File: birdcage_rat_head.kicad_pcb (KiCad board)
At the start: 2 copper layers, 131.9 x 63.3 mm, 40 parts, among them J1 Conn_Coaxial_0, J2 Conn_Coaxial_90

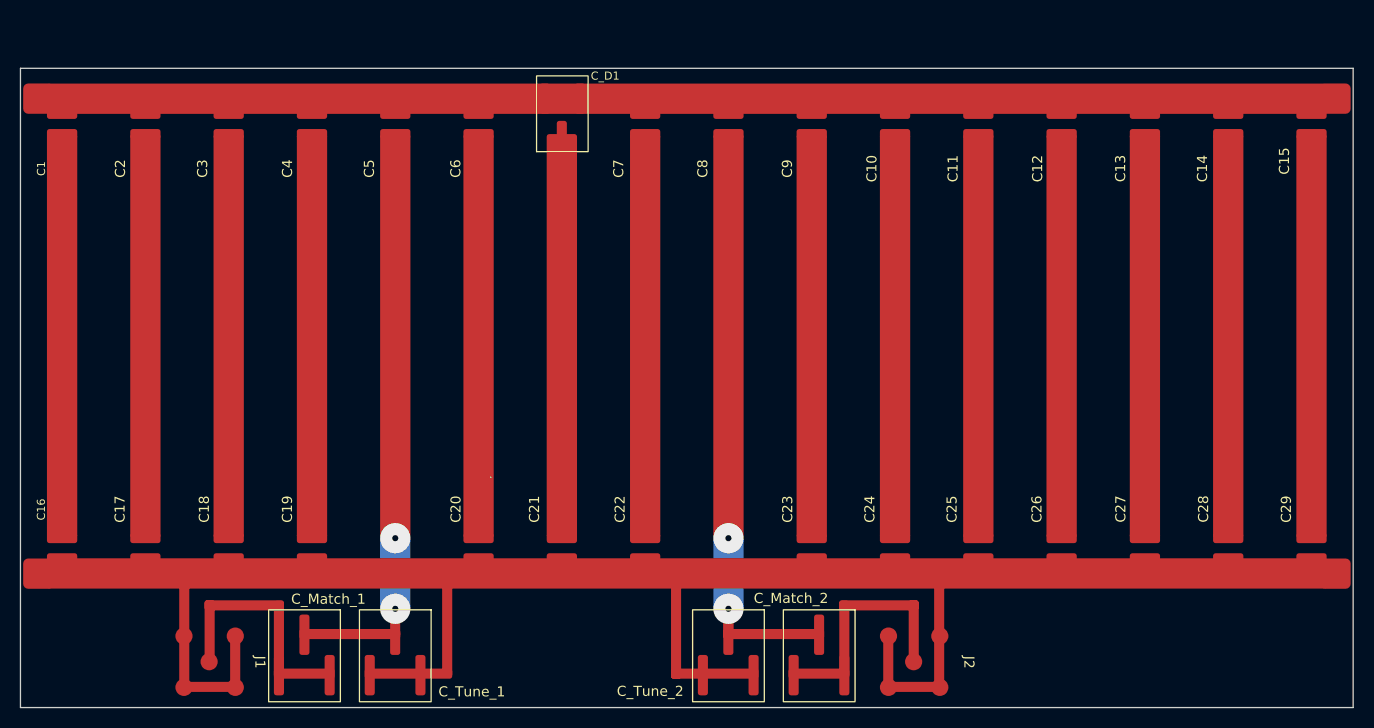
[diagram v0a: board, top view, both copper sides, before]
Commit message: Accounted for PCB thickness and reduced gap between flange and pcb
Gap was reduced so that more of the rat brain is in the coil.
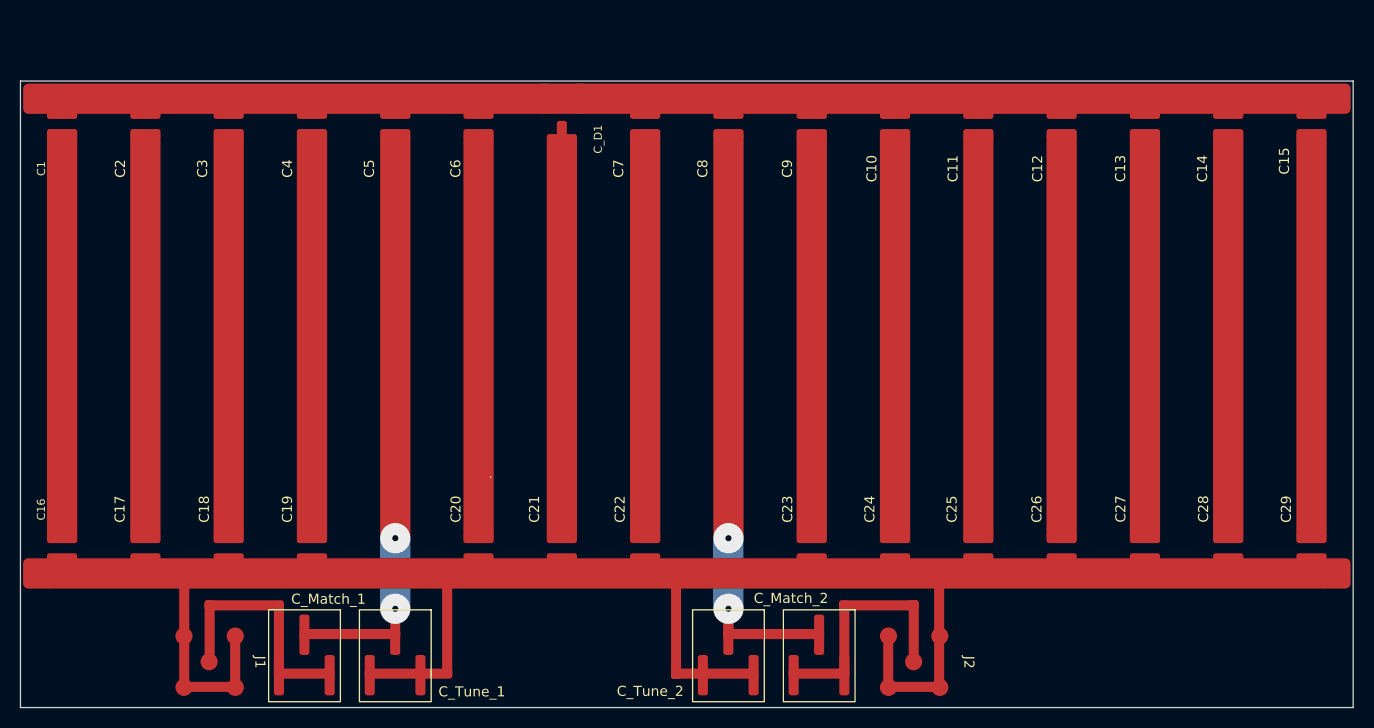
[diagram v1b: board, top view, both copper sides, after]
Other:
- board size 131.9 x 63.3 mm -> 131.9 x 62 mm
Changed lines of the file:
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@@
 	(footprint "custom_footprints:pad"
 		(layer "F.Cu")
-		(at 64.24 44.31)
+		(at 64.24 44.32)
 		(property "Reference" "REF**"
 			(at 0 -0.5 0)
@@
 	(footprint "custom_footprints:pad"
 		(layer "F.Cu")
-		(at 64.24 91.34)
+		(at 64.23 91.32)
 		(property "Reference" "REF**"
 			(at 0 -0.5 0)
@@
 	(footprint "custom_footprints:pad"
 		(layer "F.Cu")
-		(at 192.67 91.34)
+		(at 192.66 91.32)
 		(property "Reference" "REF**"
 			(at 0 -0.5 0)
@@
 		(fp_rect
 			(start 0 0)
-			(end 7.5 5.1)
+			(end 12.1 5.1)
 			(stroke
 				(width 0.1)
@@
 			)
 			(fill no)
-			(layer "F.SilkS")
+			(layer "Dwgs.User")
 		)
 		(fp_rect
 			(start 0 0)
-			(end 12.1 5.1)
+			(end 7.5 5.1)
 			(stroke
 				(width 0.1)
@@
 			)
 			(fill no)
-			(layer "Dwgs.User")
+			(layer "F.CrtYd")
 		)
 		(fp_text user "${REFERENCE}"
-			(at 7.5 6.790656 0)
+			(at 1.23 6.09 90)
 			(unlocked yes)
 			(layer "F.SilkS")
@@
 	(footprint "custom_footprints:pad"
 		(layer "F.Cu")
-		(at 192.67 44.31)
+		(at 192.67 44.32)
 		(property "Reference" "REF**"
 			(at 0 -0.5 0)
@@
 	)
 	(gr_rect
-		(start 62.469979 41.308)
+		(start 62.469979 42.57)
 		(end 194.41687 104.598)
 		(stroke

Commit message: First printing
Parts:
- moved C1 6.00 mm to (66.6, 40.8)
- moved C10 6.00 mm to (149.1, 40.8)
- moved C11 6.00 mm to (157.3, 40.8)
- moved C12 6.00 mm to (165.6, 40.8)
- moved C13 6.00 mm to (173.8, 40.8)
- moved C14 6.00 mm to (182.0, 40.8)
- moved C15 6.00 mm to (190.3, 40.8)
- moved C2 6.00 mm to (74.8, 40.8)
- moved C3 6.00 mm to (83.1, 40.8)
- moved C4 6.00 mm to (91.3, 40.8)
- moved C5 6.00 mm to (99.6, 40.8)
- moved C6 6.00 mm to (107.8, 40.8)
- moved C7 6.00 mm to (124.3, 40.8)
- moved C8 6.00 mm to (132.6, 40.8)
- moved C9 6.00 mm to (140.8, 40.8)
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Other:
- board size 131.9 x 62 mm -> 131.9 x 67.8 mm
